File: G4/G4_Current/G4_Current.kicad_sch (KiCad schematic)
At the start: 26 parts, among them J1 Conn_01x06_Socket, J2 Conn_01x06_Socket, U1 NUCLEO-G491RE, U2 INA3221_Module, U3 INA3221_Module

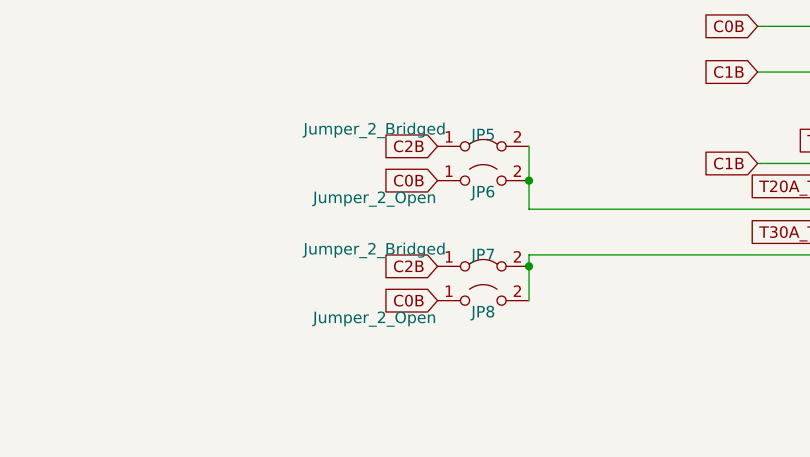
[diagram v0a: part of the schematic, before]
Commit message: fix some connectors
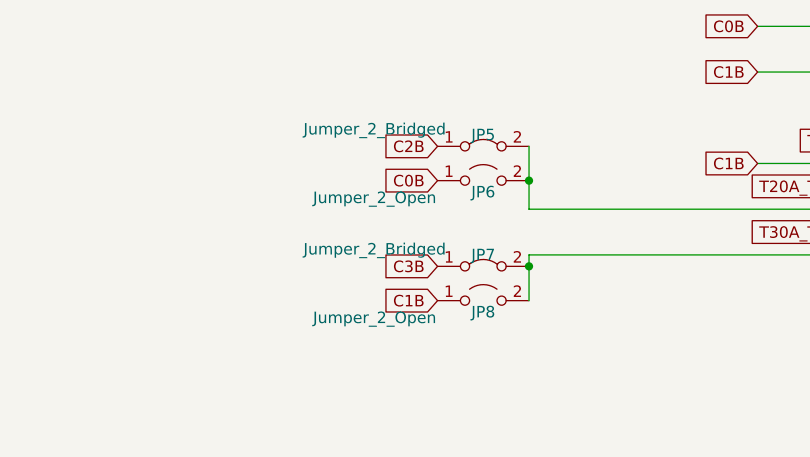
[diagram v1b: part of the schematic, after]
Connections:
- net C0B: no longer JP8.1 (A)
- net C1B: now also JP8.1 (A)
- net C2B: no longer JP7.1 (A)
- net C3B: now also JP7.1 (A)
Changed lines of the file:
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@@
     )
   )
-  (global_label "C2B" (shape input) (at 129.54 222.25 180) (fields_autoplaced)
+  (global_label "C3B" (shape input) (at 129.54 222.25 180) (fields_autoplaced)
     (effects (font (size 1.27 1.27)) (justify right))
     (property "Intersheetrefs" "${INTERSHEET_REFS}" (at 122.8053 222.25 0)
@@
     )
   )
-  (global_label "C0B" (shape input) (at 129.54 226.06 180) (fields_autoplaced)
+  (global_label "C1B" (shape input) (at 129.54 226.06 180) (fields_autoplaced)
     (effects (font (size 1.27 1.27)) (justify right))
     (property "Intersheetrefs" "${INTERSHEET_REFS}" (at 122.8053 226.06 0)

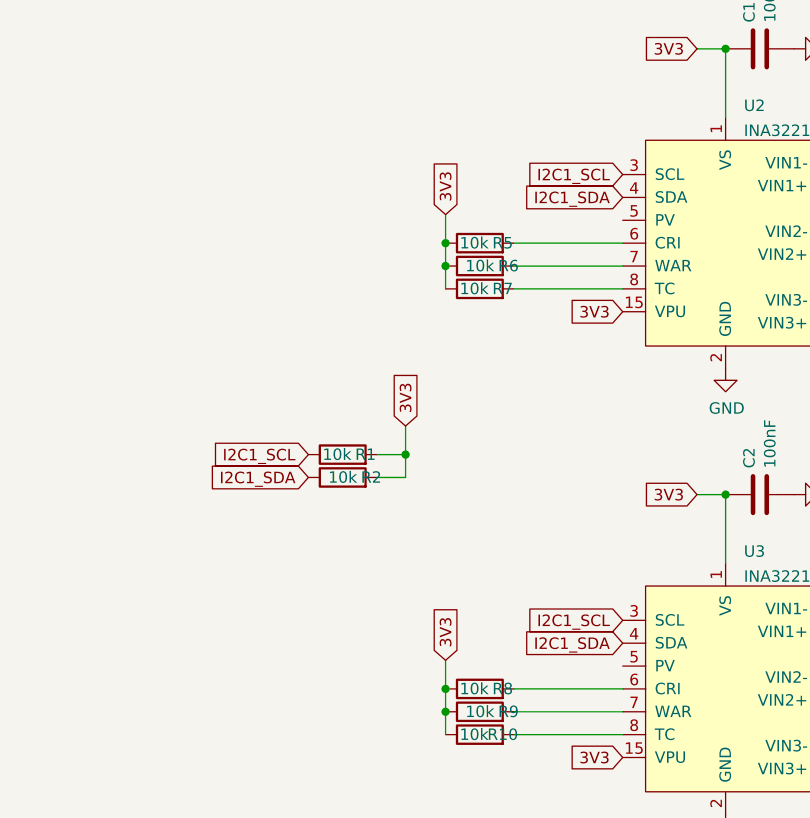
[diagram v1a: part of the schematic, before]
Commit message: change i2c1 and i2c3 for better routing
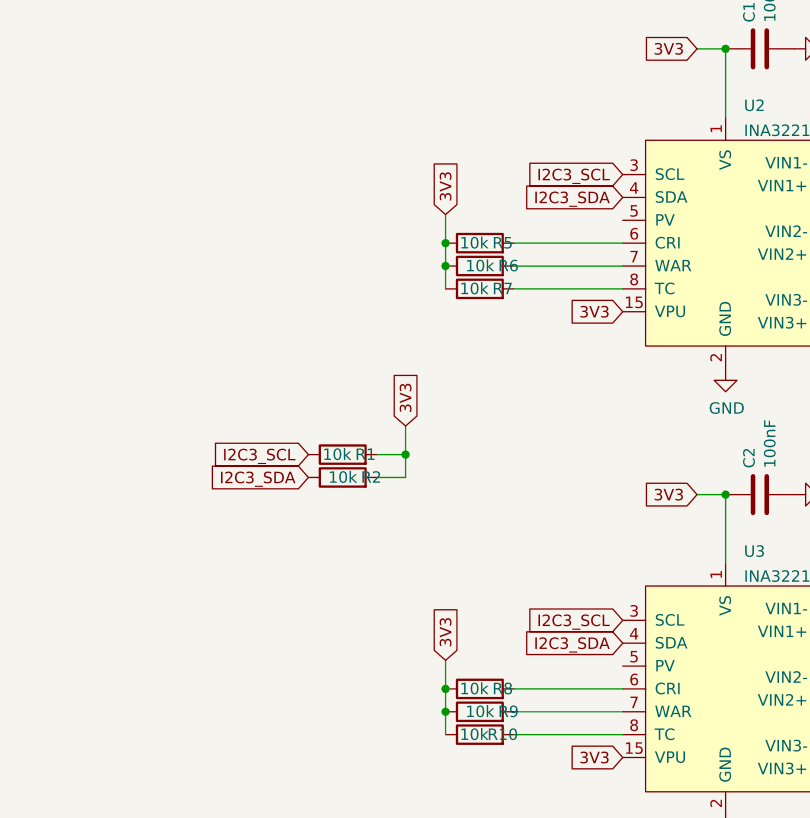
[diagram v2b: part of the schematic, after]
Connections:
- net I2C1_SCL: no longer R1.1, U2.3 (SCL), U3.3 (SCL)
- net I2C1_SDA: no longer R2.1, U2.4 (SDA), U3.4 (SDA)
- net I2C3_SCL: now also R1.1, U2.3 (SCL), U3.3 (SCL)
- net I2C3_SDA: now also R2.1, U2.4 (SDA), U3.4 (SDA)
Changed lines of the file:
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@@
     )
   )
-  (global_label "I2C1_SCL" (shape input) (at 268.605 47.625 180) (fields_autoplaced)
+  (global_label "I2C3_SCL" (shape input) (at 268.605 47.625 180) (fields_autoplaced)
     (effects (font (size 1.27 1.27)) (justify right))
     (property "Intersheetrefs" "${INTERSHEET_REFS}" (at 256.8508 47.625 0)
@@
     )
   )
-  (global_label "I2C1_SDA" (shape input) (at 268.605 99.695 180) (fields_autoplaced)
+  (global_label "I2C3_SDA" (shape input) (at 268.605 99.695 180) (fields_autoplaced)
     (effects (font (size 1.27 1.27)) (justify right))
     (property "Intersheetrefs" "${INTERSHEET_REFS}" (at 256.7903 99.695 0)
@@
     )
   )
-  (global_label "I2C1_SDA" (shape input) (at 268.605 50.165 180) (fields_autoplaced)
+  (global_label "I2C3_SDA" (shape input) (at 268.605 50.165 180) (fields_autoplaced)
     (effects (font (size 1.27 1.27)) (justify right))
     (property "Intersheetrefs" "${INTERSHEET_REFS}" (at 256.7903 50.165 0)
@@
     )
   )
-  (global_label "I2C1_SDA" (shape input) (at 233.68 81.28 180) (fields_autoplaced)
+  (global_label "I2C3_SDA" (shape input) (at 233.68 81.28 180) (fields_autoplaced)
     (effects (font (size 1.27 1.27)) (justify right))
     (property "Intersheetrefs" "${INTERSHEET_REFS}" (at 221.8653 81.28 0)
@@
     )
   )
-  (global_label "I2C1_SCL" (shape input) (at 233.68 78.74 180) (fields_autoplaced)
+  (global_label "I2C3_SCL" (shape input) (at 233.68 78.74 180) (fields_autoplaced)
     (effects (font (size 1.27 1.27)) (justify right))
     (property "Intersheetrefs" "${INTERSHEET_REFS}" (at 221.9258 78.74 0)
@@
     )
   )
-  (global_label "I2C1_SCL" (shape input) (at 268.605 97.155 180) (fields_autoplaced)
+  (global_label "I2C3_SCL" (shape input) (at 268.605 97.155 180) (fields_autoplaced)
     (effects (font (size 1.27 1.27)) (justify right))
     (property "Intersheetrefs" "${INTERSHEET_REFS}" (at 256.8508 97.155 0)
